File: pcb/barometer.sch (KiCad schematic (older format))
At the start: 3 parts, among them IC601 MS5611-01BA03

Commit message: last commit before reloading net list
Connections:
- wire segments 17 -> 15
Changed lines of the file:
@@
 BARO_CS
 Wire Wire Line
-	3700 2250 3800 2250
-Wire Wire Line
-	3800 2250 3850 2250
+	3700 2250 3850 2250
 Wire Wire Line
 	3800 2450 3900 2450
@@
 $EndComp
 $Comp
-L +3.3V #PWR504
+L +3.3V #PWR033
 U 1 1 565D7402
 P 2850 1900
-F 0 "#PWR504" H 2850 1750 50  0001 C CNN
+F 0 "#PWR033" H 2850 1750 50  0001 C CNN
 F 1 "+3.3V" H 2850 2040 50  0000 C CNN
 F 2 "" H 2850 1900 60  0000 C CNN
@@
 $EndComp
 $Comp
-L GND #PWR503
+L GND #PWR034
 U 1 1 565D746E
 P 2750 2150
-F 0 "#PWR503" H 2750 1900 50  0001 C CNN
+F 0 "#PWR034" H 2750 1900 50  0001 C CNN
 F 1 "GND" H 2750 2000 50  0000 C CNN
 F 2 "" H 2750 2150 60  0000 C CNN
@@
 $EndComp
 $Comp
-L GND #PWR502
+L GND #PWR035
 U 1 1 565D7486
 P 2500 2050
-F 0 "#PWR502" H 2500 1800 50  0001 C CNN
+F 0 "#PWR035" H 2500 1800 50  0001 C CNN
 F 1 "GND" H 2500 1900 50  0000 C CNN
 F 2 "" H 2500 2050 60  0000 C CNN
@@
 	2850 1950 2850 1900
 Wire Wire Line
-	2750 2150 2900 2150
-Wire Wire Line
-	2900 2150 3000 2150
+	2750 2150 3000 2150
 Wire Wire Line
 	3000 2050 2900 2050
@@
 	2500 1550 2500 1650
 $Comp
-L +3V3 #PWR505
+L +3V3 #PWR036
 U 1 1 565D777C
 P 4450 2400
-F 0 "#PWR505" H 4450 2250 50  0001 C CNN
+F 0 "#PWR036" H 4450 2250 50  0001 C CNN
 F 1 "+3V3" H 4450 2540 50  0000 C CNN
 F 2 "" H 4450 2400 60  0000 C CNN
@@
 	4200 2450 4450 2450
 $Comp
-L +3V3 #PWR501
+L +3V3 #PWR037
 U 1 1 565D78F9
 P 2500 1550
-F 0 "#PWR501" H 2500 1400 50  0001 C CNN
+F 0 "#PWR037" H 2500 1400 50  0001 C CNN
 F 1 "+3V3" H 2500 1690 50  0000 C CNN
 F 2 "" H 2500 1550 60  0000 C CNN

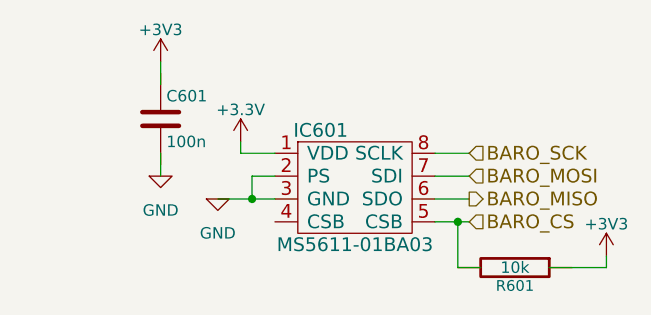
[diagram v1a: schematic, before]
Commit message: Fixed all DRC errors
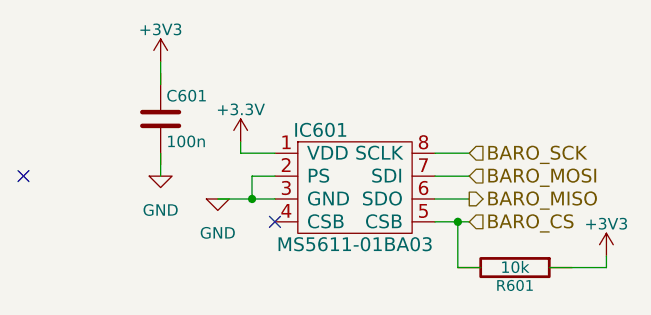
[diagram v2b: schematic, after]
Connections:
- no-connect marks 0 -> 2
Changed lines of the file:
@@
 	1    0    0    -1
 $EndComp
-Wire Wire Line
-	3700 1950 3850 1950
-Wire Wire Line
-	3700 2050 3850 2050
 Text HLabel 3850 1950 2    60   Input ~ 0
 BARO_SCK
@@
 Text HLabel 3850 2150 2    60   Output ~ 0
 BARO_MISO
-Wire Wire Line
-	3700 2150 3850 2150
 Text HLabel 3850 2250 2    60   Input ~ 0
 BARO_CS
-Wire Wire Line
-	3700 2250 3850 2250
-Wire Wire Line
-	3800 2450 3900 2450
-Wire Wire Line
-	3800 2450 3800 2250
-Connection ~ 3800 2250
 $Comp
 L R R601
@@
 	1    0    0    -1
 $EndComp
-Wire Wire Line
-	3000 1950 2850 1950
-Wire Wire Line
-	2850 1950 2850 1900
-Wire Wire Line
-	2750 2150 3000 2150
-Wire Wire Line
-	3000 2050 2900 2050
-Wire Wire Line
-	2900 2050 2900 2150
-Connection ~ 2900 2150
 $Comp
 L C C601
@@
 	1    0    0    -1
 $EndComp
-Wire Wire Line
-	2500 1950 2500 2050
-Wire Wire Line
-	2500 1550 2500 1650
 $Comp
 L +3V3 #PWR036
@@
 	1    0    0    -1
 $EndComp
-Wire Wire Line
-	4200 2450 4450 2450
 $Comp
 L +3V3 #PWR037
@@
 Wire Wire Line
 	4450 2450 4450 2400
+Wire Wire Line
+	4200 2450 4450 2450
+Wire Wire Line
+	2500 1550 2500 1650
+Wire Wire Line
+	2500 1950 2500 2050
+Connection ~ 2900 2150
+Wire Wire Line
+	2900 2050 2900 2150
+Wire Wire Line
+	3000 2050 2900 2050
+Wire Wire Line
+	2750 2150 3000 2150
+Wire Wire Line
+	2850 1950 2850 1900
+Wire Wire Line
+	3000 1950 2850 1950
+Connection ~ 3800 2250
+Wire Wire Line
+	3800 2450 3800 2250
+Wire Wire Line
+	3800 2450 3900 2450
+Wire Wire Line
+	3700 2250 3850 2250
+Wire Wire Line
+	3700 2150 3850 2150
+Wire Wire Line
+	3700 2050 3850 2050
+Wire Wire Line
+	3700 1950 3850 1950
+NoConn ~ 3000 2250
+NoConn ~ 1900 2050
 $EndSCHEMATC

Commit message: Added BOM
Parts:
- C601: symbol C -> C-RESCUE-woodchuck
- R601: symbol R -> R-RESCUE-woodchuck
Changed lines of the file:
@@
 EESchema Schematic File Version 2
+LIBS:woodchuck-rescue
 LIBS:power
 LIBS:device
@@
 LIBS:sma
 LIBS:cga0402mlc-12g
+LIBS:agg-kicad
 LIBS:woodchuck-cache
-EELAYER 27 0
+EELAYER 25 0
 EELAYER END
 $Descr A4 11693 8268
@@
 BARO_CS
 $Comp
-L R R601
+L R-RESCUE-woodchuck R601
 U 1 1 565D7136
 P 4050 2450
@@
 $EndComp
 $Comp
-L GND #PWR035
+L GND-RESCUE-woodchuck #PWR035
 U 1 1 565D746E
 P 2750 2150
@@
 $EndComp
 $Comp
-L GND #PWR036
+L GND-RESCUE-woodchuck #PWR036
 U 1 1 565D7486
 P 2500 2050
@@
 $EndComp
 $Comp
-L C C601
+L C-RESCUE-woodchuck C601
 U 1 1 565D7512
 P 2500 1800
+AR Path="/565D7512" Ref="C601"  Part="1"
+AR Path="/5657409E/565D7512" Ref="C601"  Part="1"
 F 0 "C601" H 2525 1900 50  0000 L CNN
 F 1 "100n" H 2525 1700 50  0000 L CNN

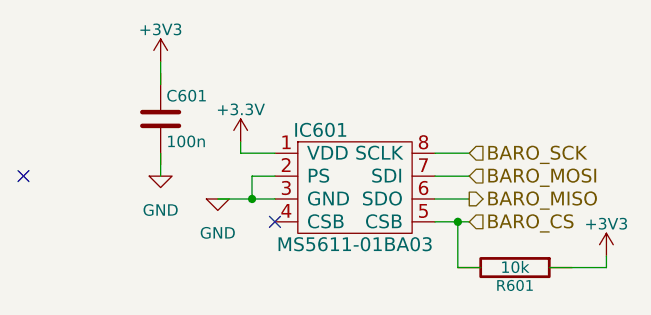
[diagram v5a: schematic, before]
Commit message: Tidy up fields to fix bom errors
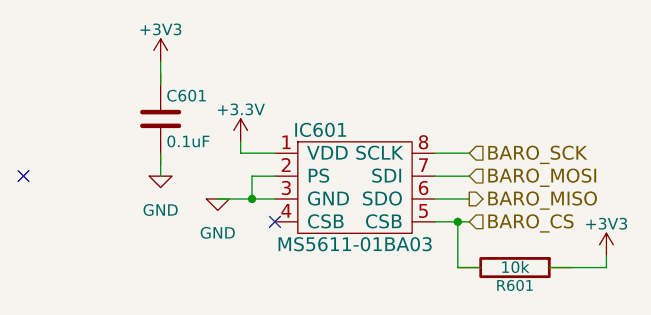
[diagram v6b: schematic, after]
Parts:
- C601: value 100n -> 0.1uF; Digikey Value -> (none); Fieldname Value -> (none)
- IC601, R601: Digikey Value -> (none); Fieldname Value -> (none)
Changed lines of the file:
@@
 F 2 "Woodchuck:MS5611-01BA" H 3600 2350 60  0001 C CNN
 F 3 "http://www.daedalus.ei.tum.de/attachments/article/61/MS5611-01BA01.pdf" H 3350 2050 60  0001 C CNN
-F 4 "Value" H 3350 2050 60  0001 C CNN "Digikey"
-F 5 "2362662" H 3350 2050 60  0001 C CNN "Farnell"
-F 6 "Value" H 3350 2050 60  0001 C CNN "Fieldname"
+F 4 "2362662" H 3350 2050 60  0001 C CNN "Farnell"
 	1    3350 2050
 	1    0    0    -1
@@
 F 2 "Woodchuck:0603" V 3980 2450 30  0001 C CNN
 F 3 "" H 4050 2450 30  0000 C CNN
-F 4 "Value" H 4050 2450 60  0001 C CNN "Digikey"
-F 5 "9331700" H 4050 2450 60  0001 C CNN "Farnell"
-F 6 "Value" H 4050 2450 60  0001 C CNN "Fieldname"
+F 4 "9331700" H 4050 2450 60  0001 C CNN "Farnell"
 	1    4050 2450
 	0    1    1    0
@@
 AR Path="/5657409E/565D7512" Ref="C601"  Part="1"
 F 0 "C601" H 2525 1900 50  0000 L CNN
-F 1 "100n" H 2525 1700 50  0000 L CNN
+F 1 "0.1uF" H 2525 1700 50  0000 L CNN
 F 2 "Woodchuck:C0603" H 2200 1800 30  0001 C CNN
 F 3 "" H 2500 1800 60  0000 C CNN
-F 4 "Value" H 2500 1800 60  0001 C CNN "Digikey"
-F 5 "1759037" H 2500 1800 60  0001 C CNN "Farnell"
-F 6 "Value" H 2500 1800 60  0001 C CNN "Fieldname"
+F 4 "1759037" H 2500 1800 60  0001 C CNN "Farnell"
 	1    2500 1800
 	1    0    0    -1
